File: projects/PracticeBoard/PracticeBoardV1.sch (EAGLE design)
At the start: 12 parts, among them U1 TPS63001

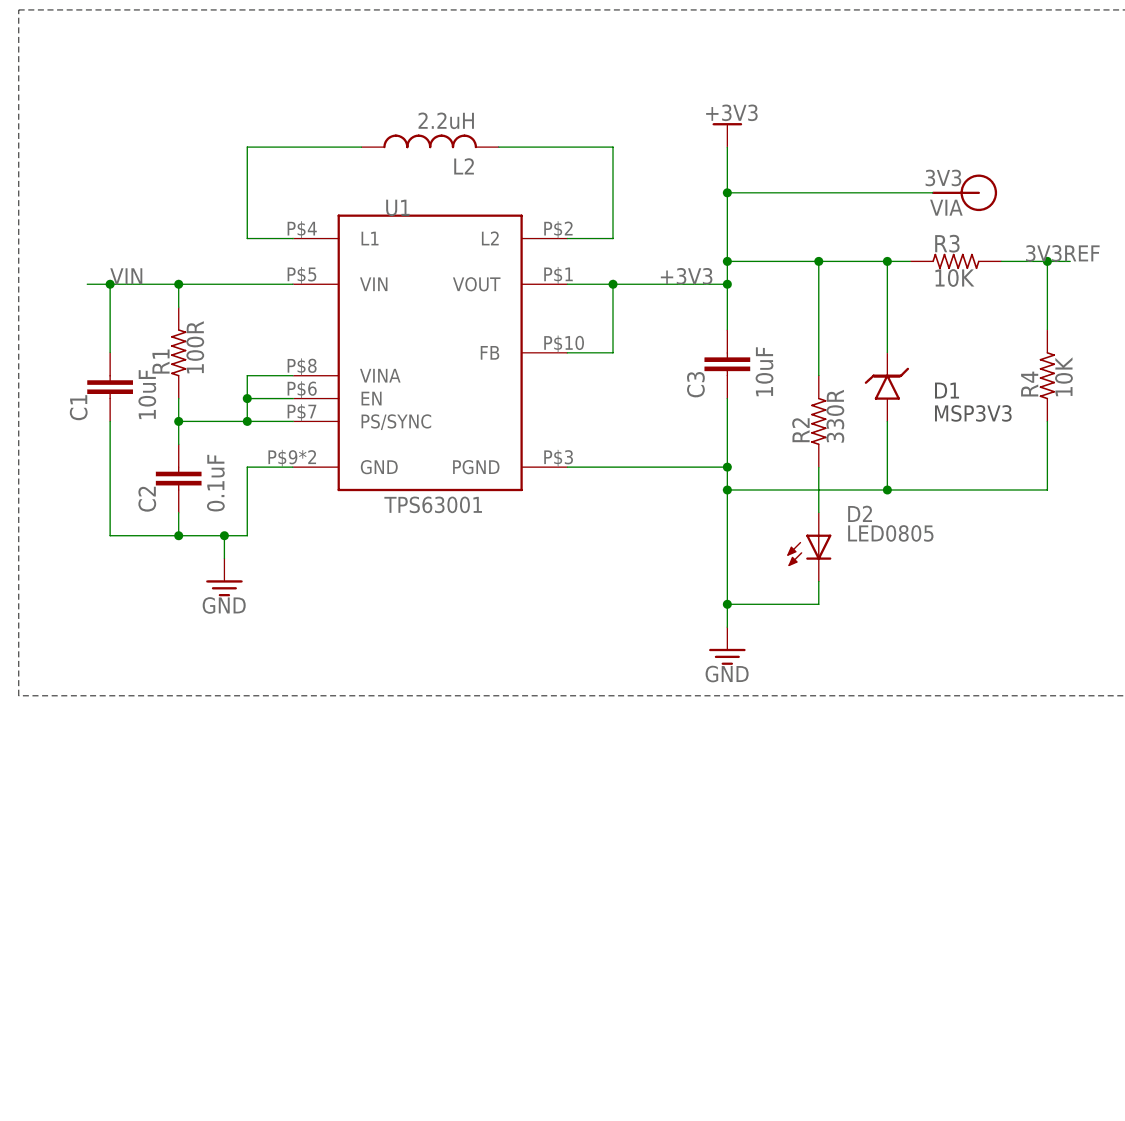
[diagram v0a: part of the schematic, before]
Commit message: Added the SN74LV04A-Hex-Inverter and corresponding package 14-TSSOP to BSE lib
>  Also worked on prepping the PracticeBoardV1 board a tiny bit
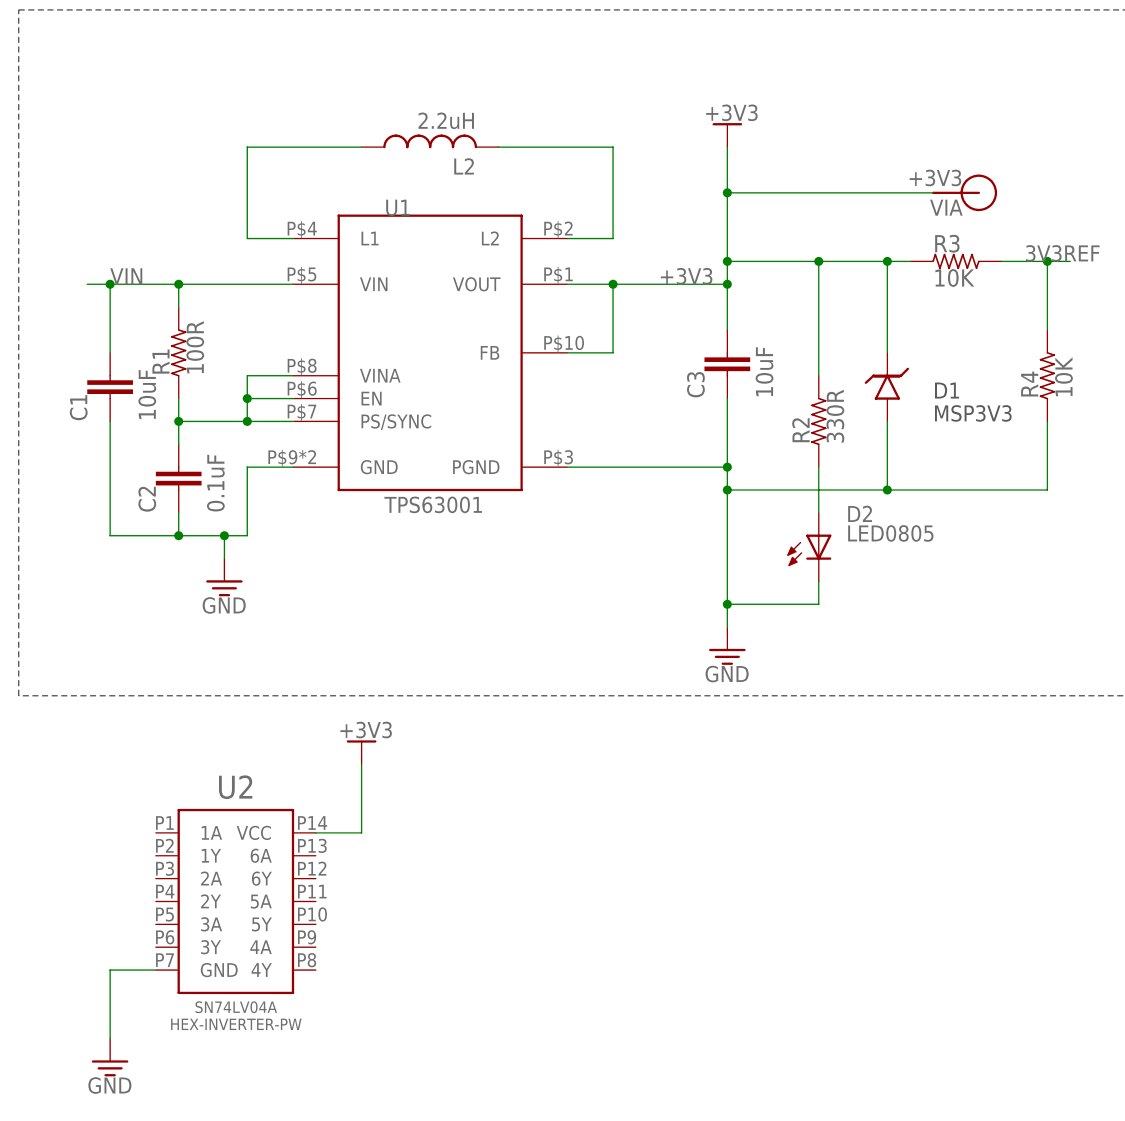
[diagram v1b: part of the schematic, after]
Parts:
- added U2: (no value), BrownSpaceEngineering:SN74LV04A-HEX-INVERTER
- V1: value 3V3 -> +3V3
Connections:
- net +3V3: now also U2.VCC
- net GND: now also U2.GND
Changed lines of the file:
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@@
 <part name="GND1" library="supply1" deviceset="GND" device=""/>
 <part name="L2" library="resistor" deviceset="L-US" device="L3225M" value="2.2uH"/>
-<part name="+3V31" library="supply1" deviceset="+3V3" device=""/>
+<part name="+3V1" library="supply1" deviceset="+3V3" device=""/>
 <part name="C1" library="BrownSpaceEngineering" deviceset="CAP" device="0805" value="10uF"/>
 <part name="C3" library="BrownSpaceEngineering" deviceset="CAP" device="0805" value="10uF"/>
@@
 <part name="D2" library="BrownSpaceEngineering" deviceset="LED" device="" technology="0805"/>
 <part name="R2" library="BrownSpaceEngineering" deviceset="RES" device="0805" value="330R"/>
-<part name="V1" library="BrownSpaceEngineering" deviceset="VIA" device="60MIL-SQ" value="3V3"/>
+<part name="V1" library="BrownSpaceEngineering" deviceset="VIA" device="60MIL-SQ" value="+3V3"/>
+<part name="U2" library="BrownSpaceEngineering" deviceset="SN74LV04A-HEX-INVERTER" device=""/>
+<part name="GND3" library="supply1" deviceset="GND" device=""/>
+<part name="+3V2" library="supply1" deviceset="+3V3" device=""/>
 </parts>
 <sheets>
@@
 <attribute name="VALUE" x="50.8" y="64.77" size="1.778" layer="96" rot="R180"/>
 </instance>
-<instance part="+3V31" gate="G$1" x="78.74" y="63.5"/>
+<instance part="+3V1" gate="G$1" x="78.74" y="63.5"/>
 <instance part="C1" gate="G$1" x="10.16" y="33.02"/>
 <instance part="C3" gate="G$1" x="78.74" y="35.56"/>
@@
 <instance part="R2" gate="R$1" x="88.9" y="30.48" rot="R90"/>
 <instance part="V1" gate="G$1" x="106.68" y="55.88" rot="R180"/>
+<instance part="U2" gate="G$1" x="15.24" y="-33.02"/>
+<instance part="GND3" gate="1" x="10.16" y="-40.64"/>
+<instance part="+3V2" gate="G$1" x="38.1" y="-5.08"/>
 </instances>
 <busses>
@@
 <segment>
 <pinref part="U1" gate="G$1" pin="VOUT"/>
-<pinref part="+3V31" gate="G$1" pin="+3V3"/>
+<pinref part="+3V1" gate="G$1" pin="+3V3"/>
 <wire x1="60.96" y1="45.72" x2="66.04" y2="45.72" width="0.1524" layer="91"/>
 <wire x1="66.04" y1="45.72" x2="78.74" y2="45.72" width="0.1524" layer="91"/>
@@
 <junction x="78.74" y="55.88"/>
 </segment>
+<segment>
+<pinref part="U2" gate="G$1" pin="VCC"/>
+<pinref part="+3V2" gate="G$1" pin="+3V3"/>
+<wire x1="33.02" y1="-15.24" x2="38.1" y2="-15.24" width="0.1524" layer="91"/>
+<wire x1="38.1" y1="-15.24" x2="38.1" y2="-7.62" width="0.1524" layer="91"/>
+</segment>
 </net>
 <net name="VIN" class="0">
@@
 <junction x="78.74" y="10.16"/>
 </segment>
+<segment>
+<pinref part="U2" gate="G$1" pin="GND"/>
+<pinref part="GND3" gate="1" pin="GND"/>
+<wire x1="15.24" y1="-30.48" x2="10.16" y2="-30.48" width="0.1524" layer="91"/>
+<wire x1="10.16" y1="-30.48" x2="10.16" y2="-38.1" width="0.1524" layer="91"/>
+</segment>
 </net>
 <net name="3V3REF" class="0">
@@
 </schematic>
 </drawing>
+<compatibility>
+<note version="6.3" minversion="6.2.2" severity="warning">
+Since Version 6.2.2 text objects can contain more than one line,
+which will not be processed correctly with this version.
+</note>
+</compatibility>
 </eagle>

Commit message: Added coin battery holder to lib; Added astable timer and AND/OR led circuit to PracticeBoardV1
Still need the LED enable circuit from ControlBoard ???
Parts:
- added BATTERY: BC-2003-COIN-BATTERY-HOLDER, BrownSpaceEngineering:BC-2003-COIN-BATTERY-HOLDER
- added C4: 0.01uF, BrownSpaceEngineering:CAP0805
- added C5: (no value), BrownSpaceEngineering:CAP0805
- added D3, D4, D5: LED0805, BrownSpaceEngineering:LED0805
- added POTENTIOMETER-IN, POTENTIOMETER-OUT: (no value), BrownSpaceEngineering:VIA60MIL-SQ
- added R5: (no value), BrownSpaceEngineering:RES1210
- added R7: (no value), BrownSpaceEngineering:RES0805
- added U3: SNX4AHC08-QUAD-2IN-AND, BrownSpaceEngineering:SNX4AHC08-QUAD-2IN-AND
- added U4: SN74LV32A-QUAD-2IN-OR, BrownSpaceEngineering:SN74LV32A-QUAD-2IN-OR
- added V2: OUT1, BrownSpaceEngineering:VIA60MIL-SQ
- added V3: IN2, BrownSpaceEngineering:VIA60MIL-SQ
- added V4: OUT2, BrownSpaceEngineering:VIA60MIL-SQ
- added V5: IN1, BrownSpaceEngineering:VIA60MIL-SQ
- added V6: IN3, BrownSpaceEngineering:VIA60MIL-SQ
- added V7: OUT3, BrownSpaceEngineering:VIA60MIL-SQ
- U2: device BrownSpaceEngineering:SN74LV04A-HEX-INVERTER -> BrownSpaceEngineering:TLC555
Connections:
- new net N$1: D3.A, U2.OUT
- new net N$10: U3.1Y, U3.2A
- new net N$11: U3.2B, U4.2B, V7.P$1
- new net N$12: D4.A, U3.2Y
- new net N$13: U4.1Y, U4.2A
- new net N$14: D5.A, U4.2Y
- new net N$2: C4.P$1, U2.CV
- new net N$3: C5.P$1, POTENTIOMETER-IN.P$1, U2.THRSH, U2.TRIG
- new net N$4: U3.1A, U4.1A, V2.P$1
- new net N$7: POTENTIOMETER-OUT.P$1, R7.1, U2.DISG
- new net N$8: U3.1B, U4.1B, V4.P$1
- net +3V3: now also R7.2, U2.RST, U3.VCC, U4.VCC, V3.P$1, V5.P$1, V6.P$1
- net GND: now also BATTERY.GND, C4.P$2, C5.P$2, D3.C, D4.C, D5.C, U3.GND, U4.GND
- net VIN: now also BATTERY.PWR
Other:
- note added: "3-input AND and 3-input OR"
- note added: "Astable Timing Circuit"
- note added: "Output"
- note added: "POTENTIOMETER VIAS"

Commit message: PracticeBoardV1 Schematic Review
Added led enable circuit and nonfunctional components
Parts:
- removed R7: (no value), BrownSpaceEngineering:RES0805
- added C26: 1uF, BrownSpaceEngineering:CAP0805
- added C27, C28: 0.01uF, BrownSpaceEngineering:CAP0805
- added D6: 1N4148SOD-523F, BrownSpaceEngineering:1N4148SOD-523F
- added D7: LED0805, BrownSpaceEngineering:LED0805
- added R23: 91K, BrownSpaceEngineering:RES0805
- added R24, R25: 10K, BrownSpaceEngineering:RES0805
- added R6: (no value), BrownSpaceEngineering:RES0805
- added U5: (no value), BrownSpaceEngineering:TLC555
- added U6: SN74LV00A-QUAD-2IN-NAND, BrownSpaceEngineering:SN74LV00A-QUAD-2IN-NAND
- added U7: (no value), BrownSpaceEngineering:SN74LV04A-HEX-INVERTER
- added U8: SNX4LV86A-QUAD-2IN-XOR, BrownSpaceEngineering:SNX4LV86A-QUAD-2IN-XOR
- added U9: UA741-OP-AMP, BrownSpaceEngineering:UA741-OP-AMP
- added V8: IN4, BrownSpaceEngineering:VIA60MIL-SQ
- added V9: OUT4, BrownSpaceEngineering:VIA60MIL-SQ
- R5: device BrownSpaceEngineering:RES1210 -> BrownSpaceEngineering:RES0805
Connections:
- new net !LED_CMD!: C28.P$1, R25.2, R6.2, V9.P$1
- new net LED_SHDN: D7.A, U5.OUT
- new net N$20: C26.P$1, R23.2, U5.DISG, U5.THRSH
- new net N$23: C27.P$1, U5.CV
- new net TRIG: C28.P$2, D6.A, R24.2, U5.TRIG
- net +3V3: now also D6.C, R23.1, R24.1, R25.1, R5.2, U5.RST, U5.VCC, V8.P$1; no longer R7.2
- net GND: now also C26.P$2, C27.P$2, D7.C, R6.1, U5.GND
- net N$7: now also R5.1; no longer R7.1
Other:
- note added: "LED Enable Circuit"
- note added: "Nonfunctional Components"
- note added: "Power Supply"
- moved on the sheet: R5

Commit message: PracticeBoardV1 Schematic Review II
> Added thru-hole diode and potentiometer to library
> Added via "switch" to the battery
> Added a second battery in series (each one has end-to-end voltage of
~2V)
> Removed unnecessary components
> Fixed (?) astable timing circuit
> Added 150R resistors in series with each LED
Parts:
- removed BATTERY: BC-2003-COIN-BATTERY-HOLDER, BrownSpaceEngineering:BC-2003-COIN-BATTERY-HOLDER
- removed POTENTIOMETER-IN, POTENTIOMETER-OUT: (no value), BrownSpaceEngineering:VIA60MIL-SQ
- removed U6: SN74LV00A-QUAD-2IN-NAND, BrownSpaceEngineering:SN74LV00A-QUAD-2IN-NAND
- removed U7: (no value), BrownSpaceEngineering:SN74LV04A-HEX-INVERTER
- removed U8: SNX4LV86A-QUAD-2IN-XOR, BrownSpaceEngineering:SNX4LV86A-QUAD-2IN-XOR
- removed U9: UA741-OP-AMP, BrownSpaceEngineering:UA741-OP-AMP
- added B1, B2: BC-2003-COIN-BATTERY-HOLDER, BrownSpaceEngineering:BC-2003-COIN-BATTERY-HOLDER
- added D8: 1N914BTR-DIODE, BrownSpaceEngineering:1N914BTR-DIODE
- added R7, R8, R9: 150R, BrownSpaceEngineering:RES0805
- added V10: IN5, BrownSpaceEngineering:VIA60MIL-SQ
- added V11: OUT5, BrownSpaceEngineering:VIA60MIL-SQ
- C4: value 0.01uF -> 1nF
- C5: value (none) -> 0.1mF
- D1: value MSP3V3 -> 1N914BTR-DIODE; device BrownSpaceEngineering:TVSMSP -> BrownSpaceEngineering:1N914BTR-DIODE
- R3: value 10K -> 20K; device BrownSpaceEngineering:RES0805 -> BrownSpaceEngineering:P160KN-0QC15B20K-POTENTIOMETER
- R5: value (none) -> 10K
- R6: value (none) -> 150R
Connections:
- removed net 3V3REF: R3.2, R4.2
- new net N$15: B2.PWR, V10.P$1
- new net N$16: D8.A, R3.P$1, U2.DISG
- new net N$17: R3.1, R4.2
- new net N$18: B1.PWR, B2.GND
- new net N$19: D7.C, R6.1
- new net N$21: D5.C, R7.2
- new net N$22: D3.C, R9.2
- new net N$24: D4.C, R8.1
- new net N$25: D1.C, R4.1
- net !LED_CMD!: no longer R6.2
- net +3V3: no longer D1.C, R3.1, V8.P$1
- net GND: now also B1.GND, R6.2, R7.1, R8.2, R9.1, V8.P$1; no longer BATTERY.GND, D1.A, D3.C, D4.C, D5.C, D7.C, R4.1, R6.1
- net N$3: now also D1.A, D8.C; no longer POTENTIOMETER-IN.P$1
- net N$7: now also R3.2; no longer POTENTIOMETER-OUT.P$1, U2.DISG
- net VIN: now also V11.P$1; no longer BATTERY.PWR
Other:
- note removed: "Nonfunctional Components"
- note removed: "Output"
- note removed: "POTENTIOMETER VIAS"
- moved on the sheet: C5, D2, D3, D5, D7, R2, R4, R5, R6

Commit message: PracticeBoardV1 Board Review
Library
> Removed the quad 2in AND gate symbol and replaced with the other
generic quad 2in gate symbol
> Consolidated quad 2in gates into one symbol and device with multiple
package variants
> Changed diode to part 1N4148; added it's thru-hole package as a
package variant to the existing 1N4148 device (and changed the existing
package's name to SMD)
ControlBoardV3
> Updated the 1N4148 diode to reflect the change in the package
variant's name
PracticeBoardV1
> Minor changes to schematic
> Board layout started and finished
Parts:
- removed B2: BC-2003-COIN-BATTERY-HOLDER, BrownSpaceEngineering:BC-2003-COIN-BATTERY-HOLDER
- added V12: LED_SHDN, BrownSpaceEngineering:VIA60MIL-SQ
- added V13: ASTABLE_OUT, BrownSpaceEngineering:VIA60MIL-SQ
- B1: value BC-2003-COIN-BATTERY-HOLDER -> Use BR2032 - 3V (2V END POINT); device BrownSpaceEngineering:BC-2003-COIN-BATTERY-HOLDER -> BrownSpaceEngineering:BC-2003-COIN-BAT-HOLDER
- D1, D8: value 1N914BTR-DIODE -> 1N4148THRU-HOLE; device BrownSpaceEngineering:1N914BTR-DIODE -> BrownSpaceEngineering:1N4148THRU-HOLE
- D6: value 1N4148SOD-523F -> 1N4148SOD-523FSMD; device BrownSpaceEngineering:1N4148SOD-523F -> BrownSpaceEngineering:1N4148SOD-523FSMD
- R3: device BrownSpaceEngineering:P160KN-0QC15B20K-POTENTIOMETER -> BrownSpaceEngineering:P160KN-0QC15B20K-POT
- U3: value SNX4AHC08-QUAD-2IN-AND -> AND; device BrownSpaceEngineering:SNX4AHC08-QUAD-2IN-AND -> BrownSpaceEngineering:QUAD-2IN-GATE-AND-SN74AHC08RGYR
- U4: value SN74LV32A-QUAD-2IN-OR -> OR; device BrownSpaceEngineering:SN74LV32A-QUAD-2IN-OR -> BrownSpaceEngineering:QUAD-2IN-GATE-OR-SN74LV32APWRG4
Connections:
- removed net N$15: B2.PWR, V10.P$1
- removed net N$18: B1.PWR, B2.GND
- new net ASTABLE_OUT: D3.A, U2.OUT, V13.P$1
- net GND: now also U3.3A, U3.3B, U3.4A, U3.4B, U4.3A, U4.3B, U4.4A, U4.4B
- net LED_SHDN: now also V12.P$1
- net N$1: now also B1.PWR, V10.P$1; no longer D3.A, U2.OUT
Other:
- moved on the sheet: B1, D3, D4, D5, R7, R8, R9

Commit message: Adjusted board layout for sizing. Added notes to silkscreen for ease of operation. Removed bottom silkscreen. Added 10k pull-down resistors to logic inputs.
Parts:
- added R10, R11, R12: 10K, BrownSpaceEngineering:RES0805
- V10: value IN5 -> BATT
- V11: value OUT5 -> INPUT
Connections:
- net GND: now also R10.1, R11.1, R12.1
- net N$10: now also R10.2
- net N$11: now also R11.2
- net N$12: now also R12.2
